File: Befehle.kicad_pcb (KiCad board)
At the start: 2 copper layers, 60 parts, among them J1 2PinTerminalBlocktg, J2 2PinTerminalBlocktg, J3 3PinTerminalBlocktg, J4 2PinTerminalBlocktg, J5 2PinTerminalBlocktg, P1 CONN_02X10, P2 CONN_02X10, U1 74LS14, U2 74540, U3 7400, U4 74HCT02, U5 74LS541, U6 74LS373, U7 74LS139, U8 74LS540

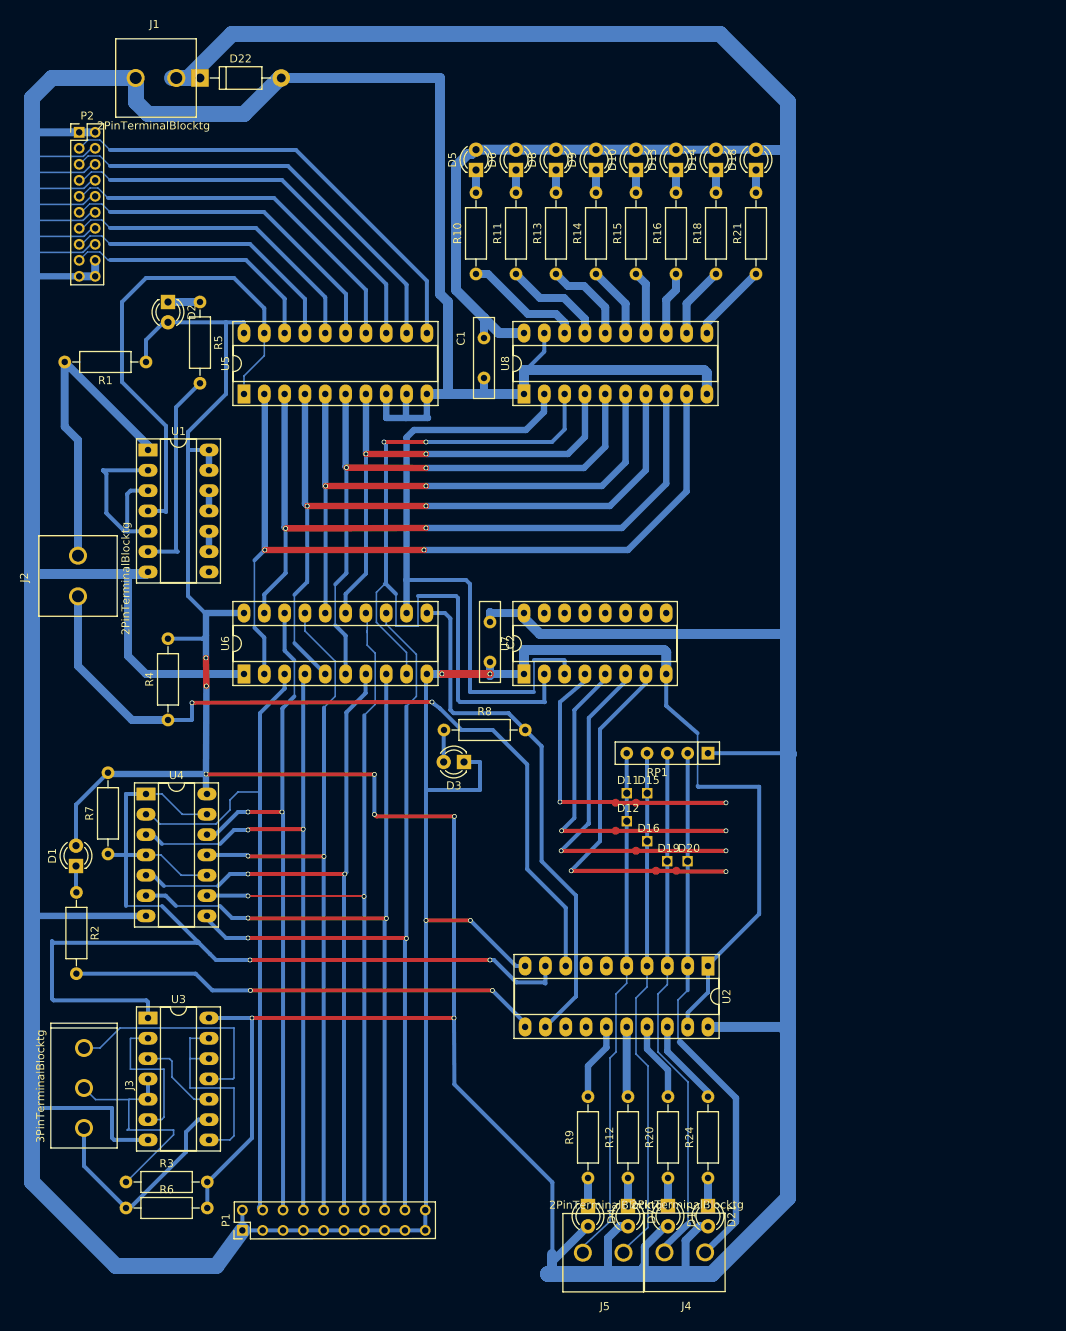
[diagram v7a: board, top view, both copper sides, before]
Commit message: footprint fertig ausgetauscht
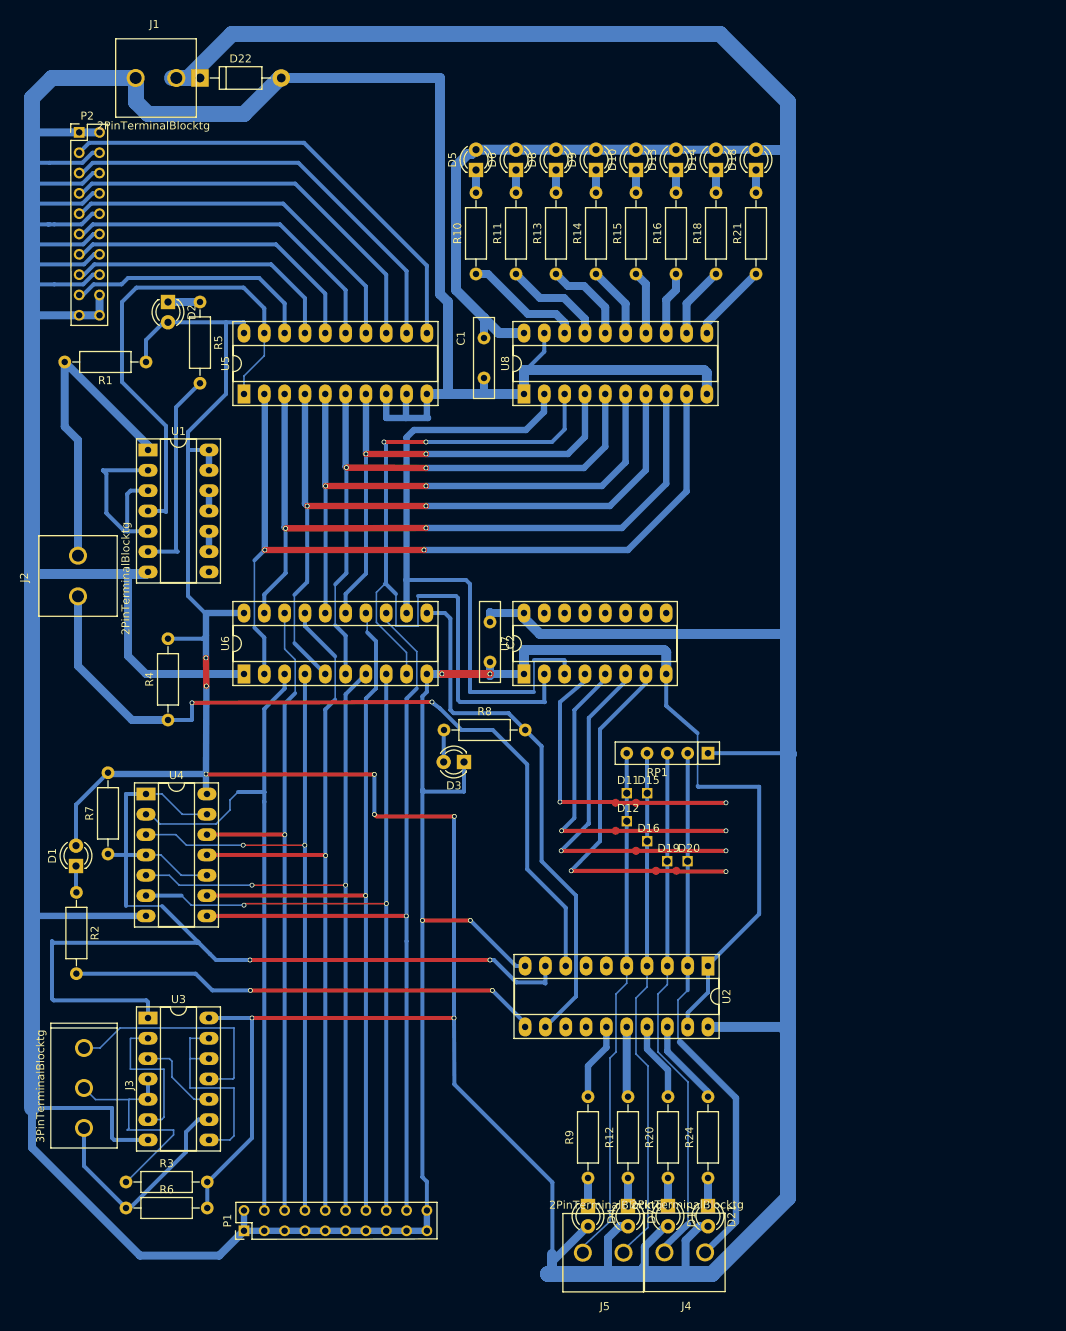
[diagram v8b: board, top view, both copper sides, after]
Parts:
- moved P1 0.21 mm to (46.0, 171.6)
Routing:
- net GND: track 698.5 -> 702.7 mm
- net Net-(P2-Pad8): track 36.6 -> 34.9 mm
- net Net-(P2-Pad7): track 40.2 -> 38.7 mm
- net Net-(P2-Pad9): track 32.8 -> 31.6 mm
- net Net-(P2-Pad2): track 57.7 -> 58.8 mm
- net Net-(U1-Pad4): track 63.2 -> 62.2 mm
- net Net-(P2-Pad5): track 47.4 -> 46.5 mm
- net /d4: track 103.1 -> 102.2 mm, vias 2 -> 1
- net Net-(P2-Pad3): track 54.1 -> 54.8 mm
- net Net-(P2-Pad6): track 43.3 -> 42.6 mm
- net /d6: track 98.3 -> 97.7 mm
- net /d7: track 88.0 -> 88.6 mm
- net /d3: track 91.5 -> 91.7 mm, vias 2 -> 1
- net /d5: track 95.7 -> 95.8 mm, vias 2 -> 1
- net /d1: track 85.7 -> 85.6 mm, vias 2 -> 1
